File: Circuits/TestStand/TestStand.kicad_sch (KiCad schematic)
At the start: 84 parts, among them J1 Screw_Terminal_01x07, J10 Screw_Terminal_01x03, J11 Screw_Terminal_01x03, J12 Screw_Terminal_01x03, J13 Screw_Terminal_01x03, J14 Screw_Terminal_01x02, J15 Conn_Coaxial, J2 Screw_Terminal_01x07, J3 Screw_Terminal_01x07, J4 Screw_Terminal_01x03, J5 Screw_Terminal_01x03, J6 Screw_Terminal_01x03, J7 Screw_Terminal_01x03, J8 Screw_Terminal_01x03, J9 Screw_Terminal_01x03, Q1 MMBT4403-7-F, Q2 MMBT4403-7-F, Q3 MMBT4403-7-F, U1 HX711, U2 HX711, U3 HX711, U4 Teensy4.1, U5 LP2980IM5X-3.3/NOPB, U6 MAX31855KASA, U7 NRF24L01, U8 LP2980IM5X-3.3/NOPB, Y1 16Mhz

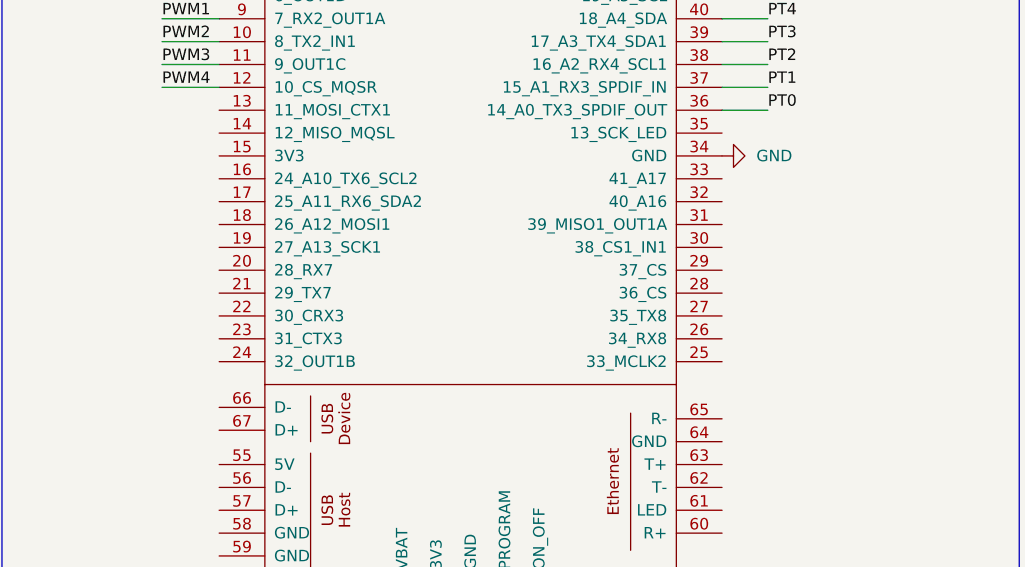
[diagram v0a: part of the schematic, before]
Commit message: Connected TC and RF to mcu
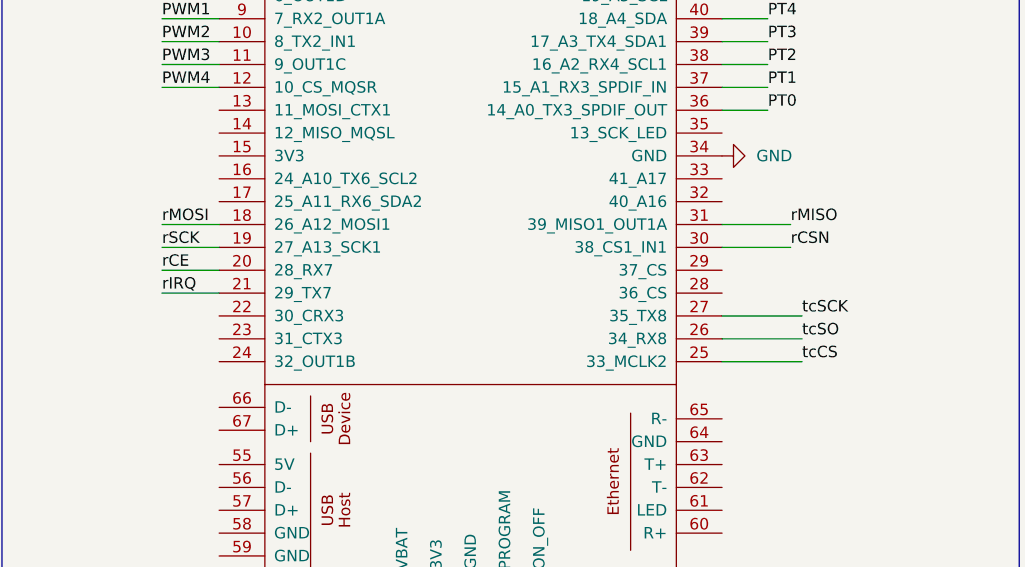
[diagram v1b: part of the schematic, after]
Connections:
- net rCE: now also U4.20 (28_RX7)
- net rCSN: now also U4.30 (38_CS1_IN1)
- net rIRQ: now also U4.21 (29_TX7)
- net rMISO: now also U4.31 (39_MISO1_OUT1A)
- net rMOSI: now also U4.18 (26_A12_MOSI1)
- net rSCK: now also U4.19 (27_A13_SCK1)
- net tcCS: now also U4.25 (33_MCLK2)
- net tcSCK: now also U4.27 (35_TX8)
- net tcSO: now also U4.26 (34_RX8)
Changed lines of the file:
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@@
+    (stroke (width 0) (type default))
+  )
+  (wire (pts (xy 34.29 219.71) (xy 40.64 219.71))
     (stroke (width 0) (type default))
   )
@@
     (stroke (width 0) (type default))
   )
+  (wire (pts (xy 34.29 222.25) (xy 40.64 222.25))
+    (stroke (width 0) (type default))
+  )
   (wire (pts (xy 163.83 193.04) (xy 175.26 193.04))
     (stroke (width 0) (type default))
@@
     (stroke (width 0) (type default))
   )
+  (wire (pts (xy 96.52 229.87) (xy 105.41 229.87))
+    (stroke (width 0) (type default))
+  )
   (wire (pts (xy 157.48 265.43) (xy 160.02 265.43))
     (stroke (width 0) (type default))
@@
     (stroke (width 0) (type default))
   )
+  (wire (pts (xy 96.52 232.41) (xy 105.41 232.41))
+    (stroke (width 0) (type default))
+  )
   (wire (pts (xy 45.72 53.34) (xy 52.07 53.34))
     (stroke (width 0) (type default))
@@
     (stroke (width 0) (type default))
   )
+  (wire (pts (xy 34.29 227.33) (xy 40.64 227.33))
+    (stroke (width 0) (type default))
+  )
   (wire (pts (xy 68.58 133.35) (xy 59.69 133.35))
     (stroke (width 0) (type default))
@@
     (stroke (width 0) (type default))
   )
+  (wire (pts (xy 34.29 224.79) (xy 40.64 224.79))
+    (stroke (width 0) (type default))
+  )
   (wire (pts (xy 35.56 49.53) (xy 35.56 53.34))
     (stroke (width 0) (type default))
@@
     (stroke (width 0) (type default))
   )
+  (wire (pts (xy 96.52 222.25) (xy 104.14 222.25))
+    (stroke (width 0) (type default))
+  )
   (wire (pts (xy 142.24 111.76) (xy 147.32 111.76))
     (stroke (width 0) (type default))
@@
     (stroke (width 0) (type default))
   )
+  (wire (pts (xy 96.52 234.95) (xy 105.41 234.95))
+    (stroke (width 0) (type default))
+  )
   (wire (pts (xy 204.47 165.1) (xy 204.47 177.8))
     (stroke (width 0) (type default))
@@
     (stroke (width 0) (type default))
   )
+  (wire (pts (xy 96.52 219.71) (xy 104.14 219.71))
+    (stroke (width 0) (type default))
+  )
   (wire (pts (xy 140.97 40.64) (xy 153.67 40.64))
     (stroke (width 0) (type default))
@@
     (effects (font (size 1.27 1.27)) (justify left bottom))
   )
+  (label "tcCS" (at 105.41 234.95 0) (fields_autoplaced)
+    (effects (font (size 1.27 1.27)) (justify left bottom))
+  )
   (label "rSCK" (at 138.43 237.49 0) (fields_autoplaced)
     (effects (font (size 1.27 1.27)) (justify left bottom))
@@
     (effects (font (size 1.27 1.27)) (justify left bottom))
   )
+  (label "tcSO" (at 105.41 232.41 0) (fields_autoplaced)
+    (effects (font (size 1.27 1.27)) (justify left bottom))
+  )
   (label "tcSCK" (at 198.12 191.77 0) (fields_autoplaced)
     (effects (font (size 1.27 1.27)) (justify left bottom))
@@
     (effects (font (size 1.27 1.27)) (justify left bottom))
   )
+  (label "rIRQ" (at 34.29 227.33 0) (fields_autoplaced)
+    (effects (font (size 1.27 1.27)) (justify left bottom))
+  )
+  (label "rSCK" (at 34.29 222.25 0) (fields_autoplaced)
+    (effects (font (size 1.27 1.27)) (justify left bottom))
+  )
+  (label "rMOSI" (at 34.29 219.71 0) (fields_autoplaced)
+    (effects (font (size 1.27 1.27)) (justify left bottom))
+  )
   (label "E1+" (at 26.67 113.03 0) (fields_autoplaced)
     (effects (font (size 1.27 1.27)) (justify left bottom))
@@
     (effects (font (size 1.27 1.27)) (justify left bottom))
   )
+  (label "rMISO" (at 104.14 219.71 0) (fields_autoplaced)
+    (effects (font (size 1.27 1.27)) (justify left bottom))
+  )
   (label "PT0" (at 101.6 207.01 0) (fields_autoplaced)
     (effects (font (size 1.27 1.27)) (justify left bottom))
@@
     (effects (font (size 1.27 1.27)) (justify left bottom))
   )
+  (label "rCE" (at 34.29 224.79 0) (fields_autoplaced)
+    (effects (font (size 1.27 1.27)) (justify left bottom))
+  )
+  (label "rCSN" (at 104.14 222.25 0) (fields_autoplaced)
+    (effects (font (size 1.27 1.27)) (justify left bottom))
+  )
   (label "rMOSI" (at 138.43 232.41 0) (fields_autoplaced)
     (effects (font (size 1.27 1.27)) (justify left bottom))
@@
     (effects (font (size 1.27 1.27)) (justify left bottom))
   )
+  (label "tcSCK" (at 105.41 229.87 0) (fields_autoplaced)
+    (effects (font (size 1.27 1.27)) (justify left bottom))
+  )

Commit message: did some traces
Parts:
- C13, C14, C15, C16, C17, C18, C19, C20, C21, C22, C23, C24, C25: footprint (none) -> Capacitor_SMD:C_0805_2012Metric
- FB1, FB2, L4, L5, L6: footprint (none) -> Inductor_SMD:L_0805_2012Metric
- J14: footprint (none) -> Connector_Wago:Wago_734-132_1x02_P3.50mm_Vertical
- J15: footprint (none) -> Connector_Coaxial:SMA_Molex_73251-1153_EdgeMount_Horizontal
- R16, R17, R18, R19: footprint (none) -> Resistor_SMD:R_0805_2012Metric
- U5, U8: footprint MF05A_TEX -> Library:MF05A_TEX
- Y1: footprint (none) -> Crystal:Crystal_SMD_2012-2Pin_2.0x1.2mm
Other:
- note added: "May need to add resistors"
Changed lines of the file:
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@@
     (effects (font (size 1.27 1.27)) (justify left bottom))
   )
+  (text "May need to add resistors\n" (at 101.6 193.04 0)
+    (effects (font (size 1.27 1.27)) (justify left bottom))
+  )
   (text "Load Cell 1 IO and Amplifier\n" (at 16.51 92.71 0)
     (effects (font (size 1.27 1.27)) (justify left bottom))
@@
       (effects (font (size 1.27 1.27)))
     )
-    (property "Footprint" "" (at 142.24 198.12 0)
+    (property "Footprint" "Connector_Wago:Wago_734-132_1x02_P3.50mm_Vertical" (at 142.24 198.12 0)
       (effects (font (size 1.27 1.27)) hide)
     )
@@
       (effects (font (size 1.27 1.27)) (justify left))
     )
-    (property "Footprint" "" (at 254 242.57 0)
+    (property "Footprint" "Connector_Coaxial:SMA_Molex_73251-1153_EdgeMount_Horizontal" (at 254 242.57 0)
       (effects (font (size 1.27 1.27)) hide)
     )
@@
       (effects (font (size 1.27 1.27)))
     )
-    (property "Footprint" "" (at 154.94 194.818 90)
+    (property "Footprint" "Inductor_SMD:L_0805_2012Metric" (at 154.94 194.818 90)
       (effects (font (size 1.27 1.27)) hide)
     )
@@
       (effects (font (size 1.524 1.524)))
     )
-    (property "Footprint" "MF05A_TEX" (at 153.67 283.21 0)
+    (property "Footprint" "Library:MF05A_TEX" (at 153.67 283.21 0)
       (effects (font (size 1.27 1.27) italic) hide)
     )
@@
       (effects (font (size 1.524 1.524)))
     )
-    (property "Footprint" "MF05A_TEX" (at 148.59 160.02 0)
+    (property "Footprint" "Library:MF05A_TEX" (at 148.59 160.02 0)
       (effects (font (size 1.27 1.27) italic) hide)
     )
@@
       (effects (font (size 1.27 1.27)) (justify left))
     )
-    (property "Footprint" "" (at 219.4052 175.26 0)
+    (property "Footprint" "Capacitor_SMD:C_0805_2012Metric" (at 219.4052 175.26 0)
       (effects (font (size 1.27 1.27)) hide)
     )
@@
       (effects (font (size 1.27 1.27)) (justify left))
     )
-    (property "Footprint" "" (at 164.7952 200.66 0)
+    (property "Footprint" "Capacitor_SMD:C_0805_2012Metric" (at 164.7952 200.66 0)
       (effects (font (size 1.27 1.27)) hide)
     )
@@
       (effects (font (size 1.27 1.27)))
     )
-    (property "Footprint" "" (at 237.7948 247.65 0)
+    (property "Footprint" "Capacitor_SMD:C_0805_2012Metric" (at 237.7948 247.65 0)
       (effects (font (size 1.27 1.27)) hide)
     )
@@
       (effects (font (size 1.27 1.27)))
     )
-    (property "Footprint" "" (at 209.55 250.4948 0)
+    (property "Footprint" "Capacitor_SMD:C_0805_2012Metric" (at 209.55 250.4948 0)
       (effects (font (size 1.27 1.27)) hide)
     )
@@
       (effects (font (size 1.27 1.27)))
     )
-    (property "Footprint" "" (at 141.224 251.714 90)
+    (property "Footprint" "Resistor_SMD:R_0805_2012Metric" (at 141.224 251.714 90)
       (effects (font (size 1.27 1.27)) hide)
     )
@@
       (effects (font (size 1.27 1.27)) (justify left))
     )
-    (property "Footprint" "" (at 233.3752 175.26 0)
+    (property "Footprint" "Capacitor_SMD:C_0805_2012Metric" (at 233.3752 175.26 0)
       (effects (font (size 1.27 1.27)) hide)
     )
@@
       (effects (font (size 1.27 1.27)))
     )
-    (property "Footprint" "" (at 193.3448 224.79 0)
+    (property "Footprint" "Capacitor_SMD:C_0805_2012Metric" (at 193.3448 224.79 0)
       (effects (font (size 1.27 1.27)) hide)
     )
@@
       (effects (font (size 1.27 1.27)))
     )
-    (property "Footprint" "" (at 207.01 232.41 0)
+    (property "Footprint" "Inductor_SMD:L_0805_2012Metric" (at 207.01 232.41 0)
       (effects (font (size 1.27 1.27)) hide)
     )
@@
       (effects (font (size 1.27 1.27)))
     )
-    (property "Footprint" "" (at 216.2048 283.21 0)
+    (property "Footprint" "Capacitor_SMD:C_0805_2012Metric" (at 216.2048 283.21 0)
       (effects (font (size 1.27 1.27)) hide)
     )
@@
       (effects (font (size 1.27 1.27)))
     )
-    (property "Footprint" "" (at 214.63 237.49 0)
+    (property "Footprint" "Inductor_SMD:L_0805_2012Metric" (at 214.63 237.49 0)
       (effects (font (size 1.27 1.27)) hide)
     )
@@
       (effects (font (size 1.27 1.27)) (justify left))
     )
-    (property "Footprint" "" (at 182.626 255.524 90)
+    (property "Footprint" "Resistor_SMD:R_0805_2012Metric" (at 182.626 255.524 90)
       (effects (font (size 1.27 1.27)) hide)
     )
@@
       (effects (font (size 1.27 1.27)))
     )
-    (property "Footprint" "" (at 181.9148 224.79 0)
+    (property "Footprint" "Capacitor_SMD:C_0805_2012Metric" (at 181.9148 224.79 0)
       (effects (font (size 1.27 1.27)) hide)
     )
@@
       (effects (font (size 1.27 1.27)) (justify left))
     )
-    (property "Footprint" "" (at 213.106 190.754 90)
+    (property "Footprint" "Resistor_SMD:R_0805_2012Metric" (at 213.106 190.754 90)
       (effects (font (size 1.27 1.27)) hide)
     )
@@
       (effects (font (size 1.27 1.27)))
     )
-    (property "Footprint" "" (at 209.55 258.1148 0)
+    (property "Footprint" "Capacitor_SMD:C_0805_2012Metric" (at 209.55 258.1148 0)
       (effects (font (size 1.27 1.27)) hide)
     )
@@
       (effects (font (size 1.27 1.27)))
     )
-    (property "Footprint" "" (at 230.1748 283.21 0)
+    (property "Footprint" "Capacitor_SMD:C_0805_2012Metric" (at 230.1748 283.21 0)
       (effects (font (size 1.27 1.27)) hide)
     )
@@
       (effects (font (size 1.27 1.27)))
     )
-    (property "Footprint" "" (at 144.78 256.8448 0)
+    (property "Footprint" "Capacitor_SMD:C_0805_2012Metric" (at 144.78 256.8448 0)
       (effects (font (size 1.27 1.27)) hide)
     )
@@
       (effects (font (size 1.27 1.27)) (justify left))
     )
-    (property "Footprint" "" (at 213.106 203.454 90)
+    (property "Footprint" "Resistor_SMD:R_0805_2012Metric" (at 213.106 203.454 90)
       (effects (font (size 1.27 1.27)) hide)
     )
@@
       (effects (font (size 1.27 1.27)))
     )
-    (property "Footprint" "" (at 222.25 242.57 0)
+    (property "Footprint" "Inductor_SMD:L_0805_2012Metric" (at 222.25 242.57 0)
       (effects (font (size 1.27 1.27)) hide)
     )
@@
       (effects (font (size 1.27 1.27)))
     )
-    (property "Footprint" "" (at 154.94 202.438 90)
+    (property "Footprint" "Inductor_SMD:L_0805_2012Metric" (at 154.94 202.438 90)
       (effects (font (size 1.27 1.27)) hide)
     )
@@
       (effects (font (size 1.27 1.27)) (justify right))
     )
-    (property "Footprint" "" (at 191.77 255.27 0)
+    (property "Footprint" "Crystal:Crystal_SMD_2012-2Pin_2.0x1.2mm" (at 191.77 255.27 0)
       (effects (font (size 1.27 1.27)) hide)
     )
@@
       (effects (font (size 1.27 1.27)))
     )
-    (property "Footprint" "" (at 233.68 241.6048 0)
+    (property "Footprint" "Capacitor_SMD:C_0805_2012Metric" (at 233.68 241.6048 0)
       (effects (font (size 1.27 1.27)) hide)
     )
@@
       (effects (font (size 1.27 1.27)))
     )
-    (property "Footprint" "" (at 223.8248 283.21 0)
+    (property "Footprint" "Capacitor_SMD:C_0805_2012Metric" (at 223.8248 283.21 0)
       (effects (font (size 1.27 1.27)) hide)
     )
